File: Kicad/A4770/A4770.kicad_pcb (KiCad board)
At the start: 4 copper layers, 175.6 x 96.4 mm, 127 parts, among them CN1 Zorro3, J1 5749721-7, J2 5749721-7, J3 TO-LED, J4 TO-MB, J5 TO-A3000-LED, J6 TO-A3000-MB, J8 Conn_01x06_Pin, U1 SN74ABT16543DGGR, U10 DS21S07A, U11 DS21S07A, U12 DS21S07A, U13 W25X40CLSN, U2 SN74ABT16543DGGR, U3 SN74ABT16543DGGR, U4 SN74ABT16543DGGR, U5 74LVC07APW_118, U6 SN74ABT16543DGGR, U7 AMS1117-3.3, U8 XC95144XL-TQ144, U9 LSI53C770 SCSI Host Controller, Y1 Abracon ACO-50MHz, Y2 Abracon ACO-40MHz

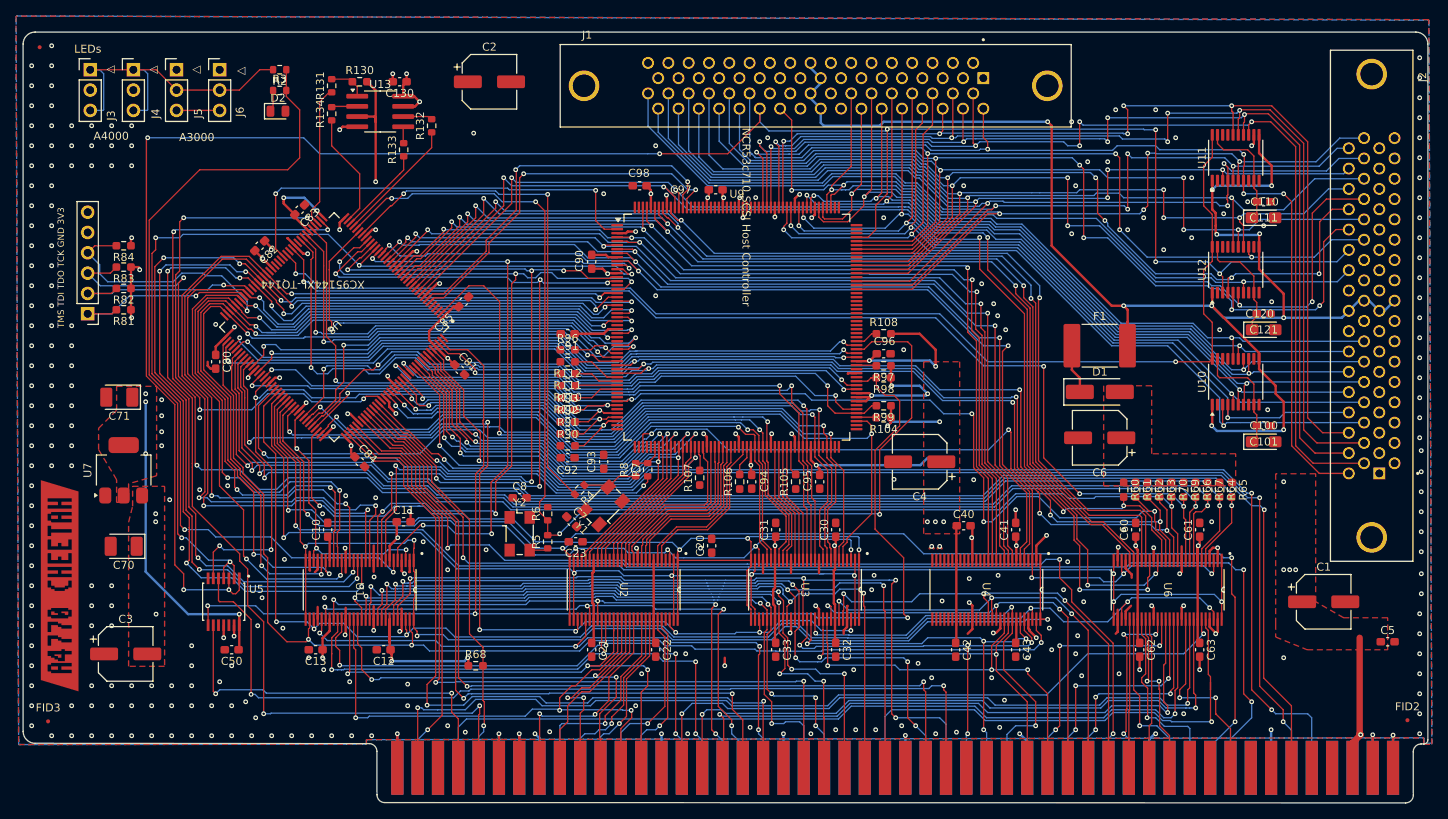
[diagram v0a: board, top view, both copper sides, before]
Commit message: CLK placement and routing
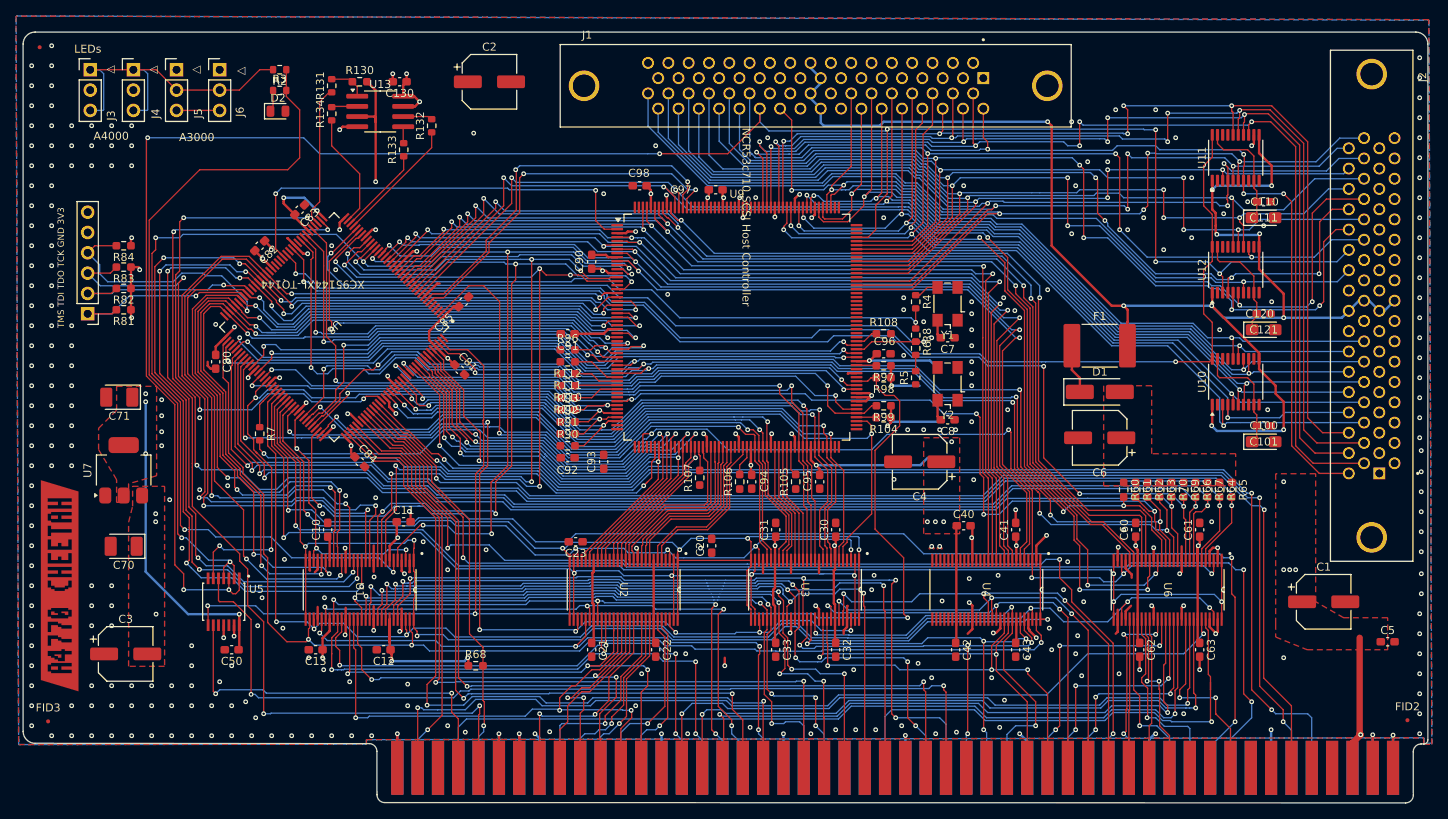
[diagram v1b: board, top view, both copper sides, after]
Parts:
- J2: value 5749721-7 -> 5787082-7
- R6, R8: value 22 -> 0
- R7: value 0 -> 22
- moved Y2 56.7 mm to (164.5, 102.3), turned to 180 degrees
- moved C8 54.4 mm to (164.5, 106.8), turned to 180 degrees
- moved C7 52.3 mm to (164.5, 96.5), turned to 180 degrees
- moved R6 50.4 mm to (160.5, 97.8), turned to -90 degrees
- moved R5 50.4 mm to (160.5, 101.5)
- moved Y1 49.8 mm to (164.5, 92.3), turned to 180 degrees
- moved R7 48.7 mm to (78.5, 108.5), turned to -90 degrees
- moved R4 48.1 mm to (160.5, 92.0), turned to -90 degrees
- moved R8 38.8 mm to (160.5, 96.2), turned to -90 degrees
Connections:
- R5 pad 2: SCLK -> Net-(R5-Pad2)
- R6 pad 2: Net-(Y1-OUT) -> Net-(R5-Pad2)
- R8 pad 1: Net-(Y1-OUT) -> BCLK_FULL
- R8 pad 2: BCLK -> SCLK
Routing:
- net BCLK: track 3.91 -> 59.0 mm, vias 0 -> 2
- net BCLK_HALF: track 60.5 -> 5.58 mm, vias 2 -> 0
- net SCLK: track 140.3 -> 93.7 mm, vias 4 -> 2
- net V3_3: track 224.4 -> 201.9 mm, vias 18 -> 17
- net BCLK_FULL: track 64.5 -> 83.6 mm
- net V5: track 245.7 -> 233.6 mm, vias 34 -> 32
- net A13: track 114.4 -> 119.2 mm
- net A14: track 115.0 -> 119.4 mm
- net Net-(Y1-OUT): track 7.08 -> 3.13 mm
- net A15: track 116.2 -> 119.8 mm
- net A10: track 114.4 -> 117.9 mm
- net A12: track 114.2 -> 117.3 mm
- net A31: track 104.5 -> 107.2 mm
- net A9: track 116.5 -> 119.1 mm
- net A30: track 106.7 -> 104.2 mm
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
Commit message: Routing
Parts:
- moved Y1 66.6 mm to (99.5, 77.5), turned to -45 degrees
- moved R4 65.9 mm to (95.5, 81.0), turned to 135 degrees
- moved C7 65.3 mm to (103.0, 74.5), turned to -45 degrees
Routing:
- net GND: track 219.4 -> 338.8 mm, vias 340 -> 346
- net BCLK_FULL: track 83.6 -> 86.8 mm
- net Net-(Y1-OUT): track 3.13 -> 0.00 mm
- net V5: track 233.6 -> 231.3 mm
- net Net-(R5-Pad2): track 2.02 -> 0.00 mm
- net D15: track 78.6 -> 76.6 mm
- net Z_CFGIN: track 153.3 -> 155.0 mm
- net PLD_DS2: track 148.1 -> 149.7 mm
- net Z2D: track 110.8 -> 112.1 mm
- net PLD_READ: track 150.2 -> 151.5 mm
- net A29: track 103.8 -> 102.7 mm
- net PLD_DS3: track 145.2 -> 146.1 mm
- net PLD_DS1: track 150.6 -> 151.5 mm
- net A21: track 118.2 -> 119.0 mm
- net A28: track 109.2 -> 108.4 mm
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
